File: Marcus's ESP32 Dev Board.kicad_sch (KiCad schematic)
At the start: 55 parts, among them J2 USB_B_Micro, J4 Conn_01x16, U1 ESP32-S3-WROOM-1, U11 BMP390, U4 MMC5983MA, U6 DRV2605LDGS, U7 DRV2605LDGS, U8 MAX17048G_T10, U9 USBLC6-2SC6

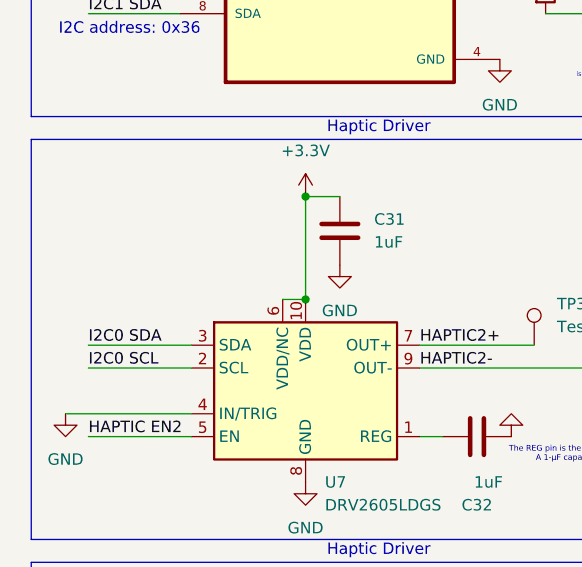
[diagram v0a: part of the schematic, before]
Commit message: feat(pcb) add pullups to I2C0, move battery sensor to I2C0
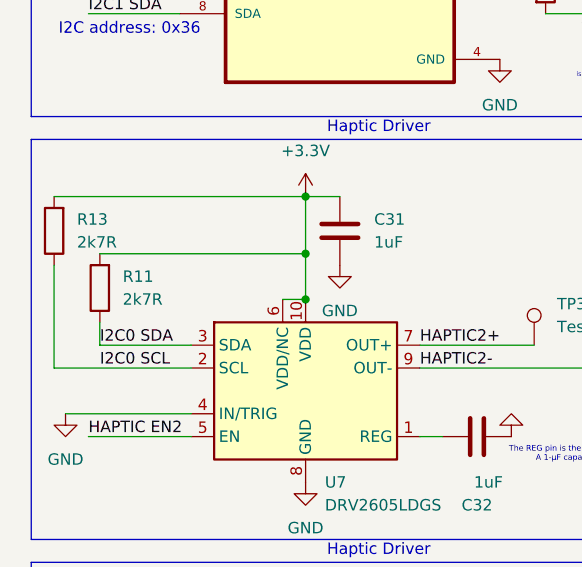
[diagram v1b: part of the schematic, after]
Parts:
- added R11, R13: 2k7R, Capacitor_SMD:C_0402_1005Metric, symbol Device:R
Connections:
- net +3.3V: now also R11.2, R13.2
- net I2C0 SCL: now also R13.1
- net I2C0 SDA: now also R11.1

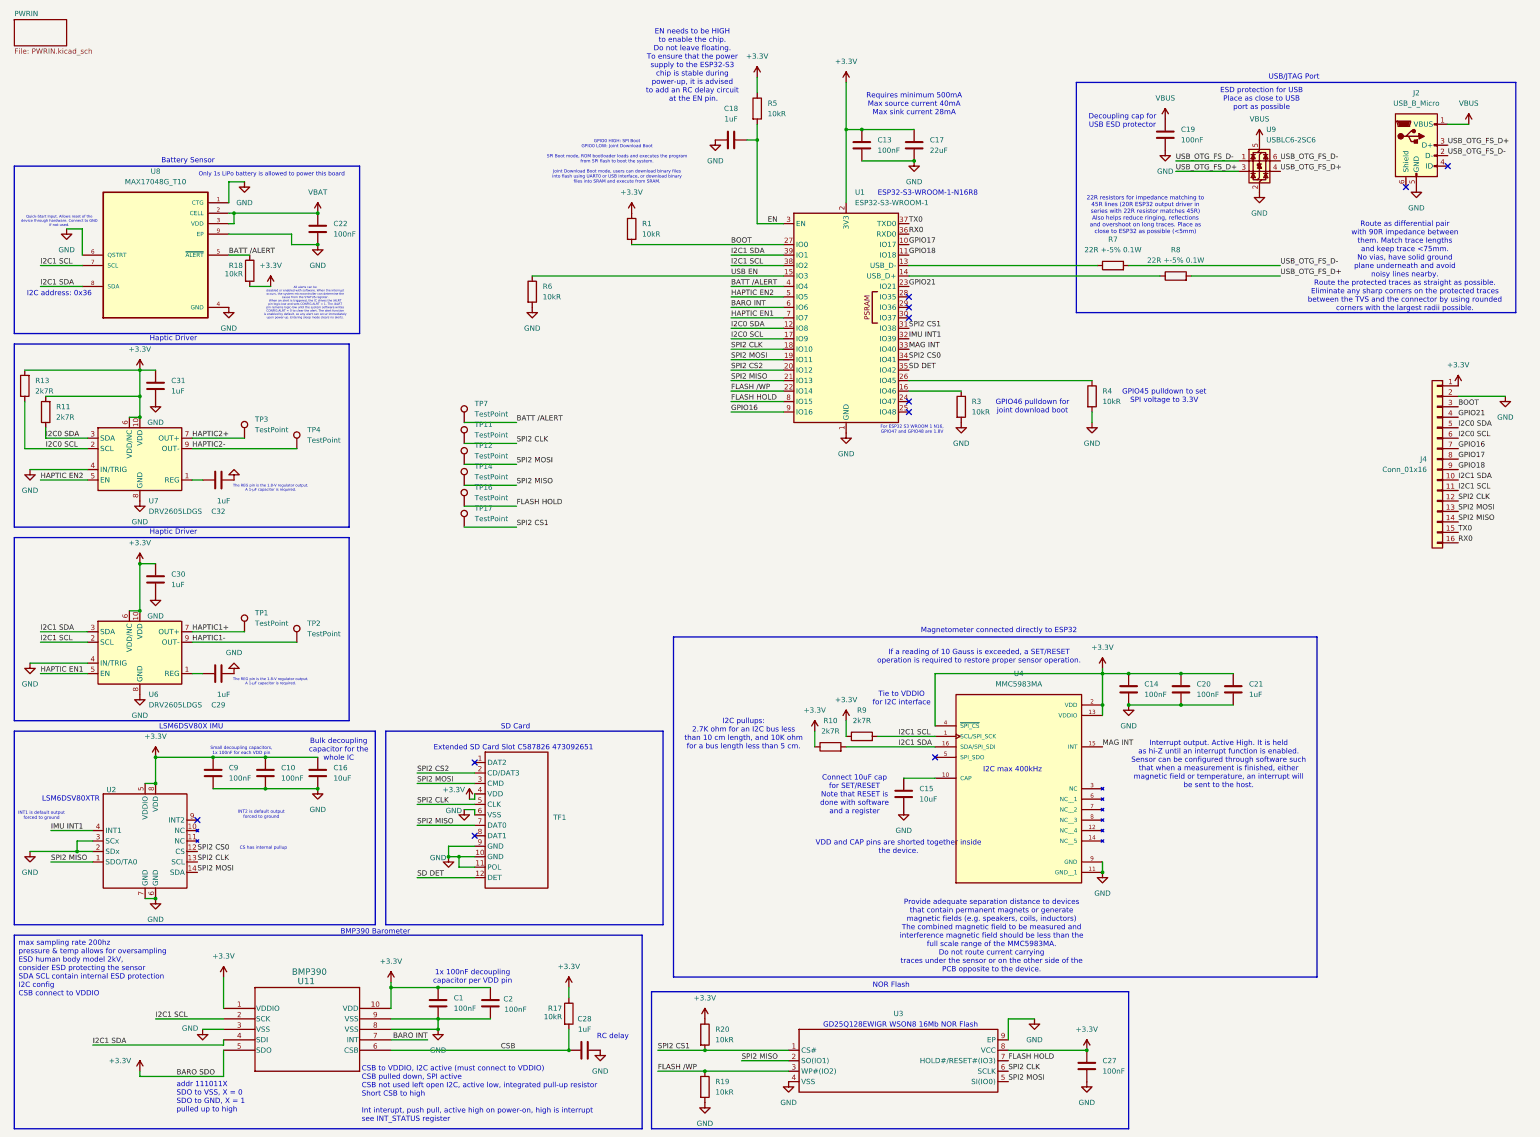
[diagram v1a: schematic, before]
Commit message: feat(pcb) cleanup and improve reliability
add pullups to SPI CS lines, rearrange board slightly, add V1.0 silkscreen, increase size of VBUS input cap
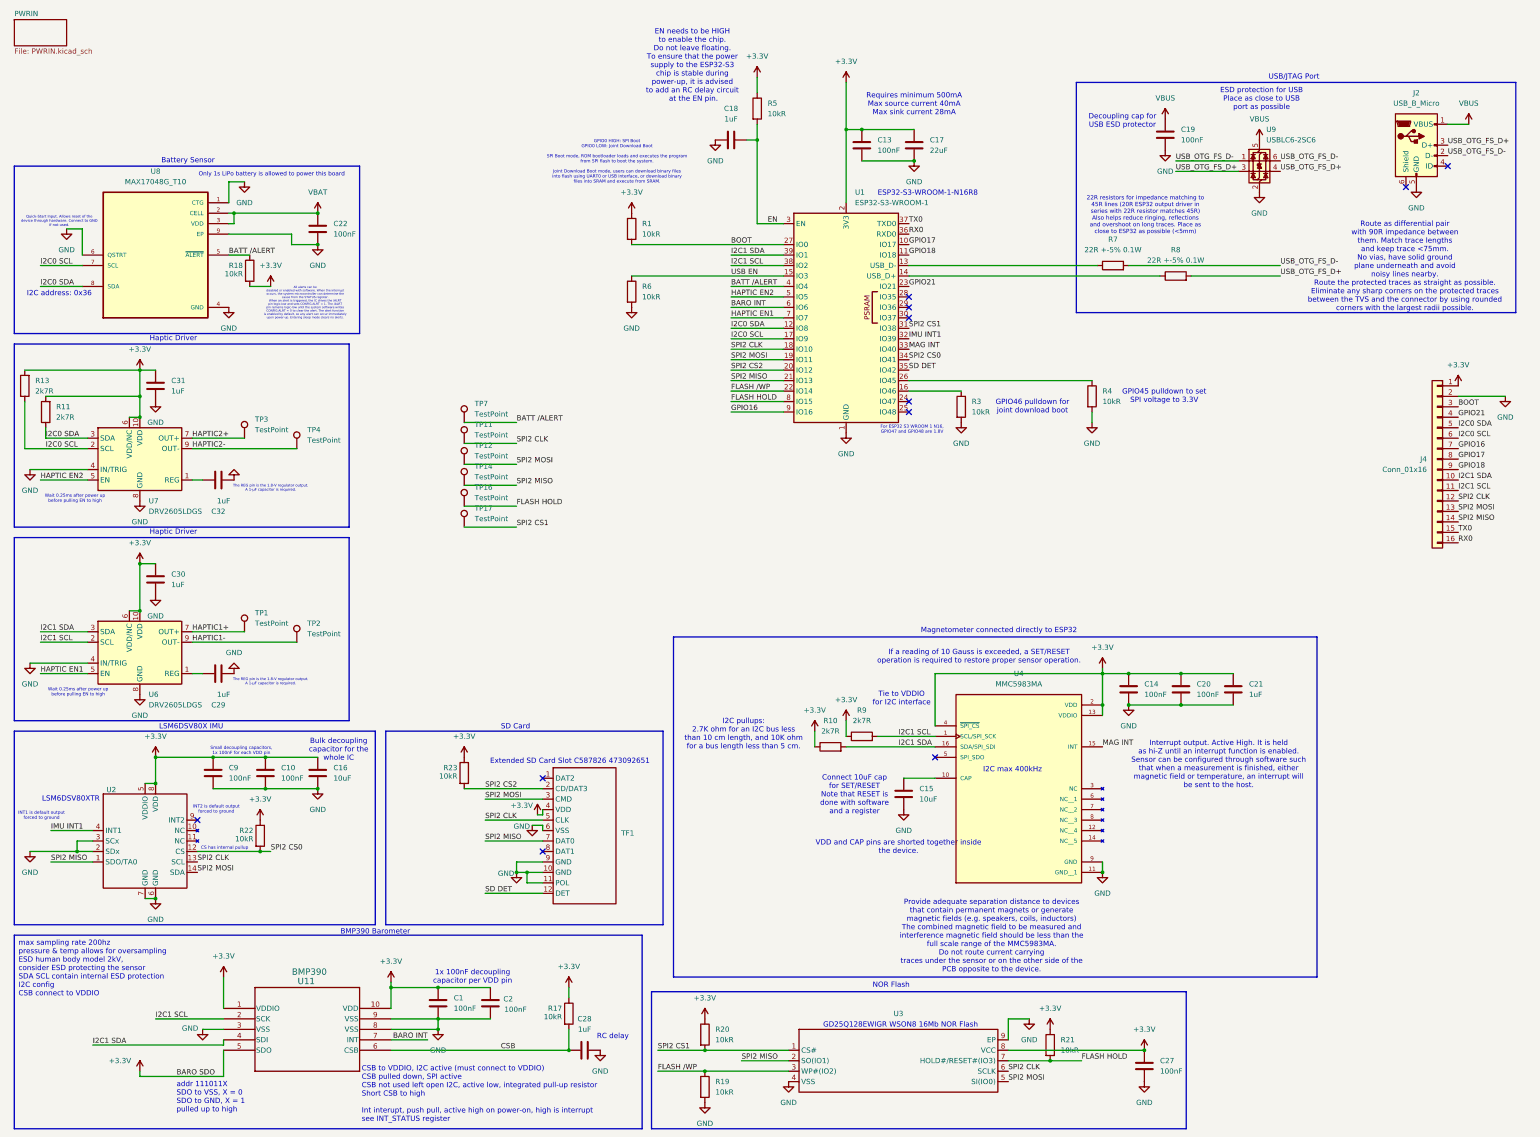
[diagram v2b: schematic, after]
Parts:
- added R21, R22, R23: 10kR, Resistor_SMD:R_0201_0603Metric, symbol Device:R
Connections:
- net +3.3V: now also R21.1, R22.1, R23.1
- net FLASH HOLD: now also R21.2
- net I2C0 SCL: now also U8.7 (SCL)
- net I2C0 SDA: now also U8.8 (SDA)
- net I2C1 SCL: no longer U8.7 (SCL)
- net I2C1 SDA: no longer U8.8 (SDA)
- net SPI2 CS0: now also R22.2
- net SPI2 CS2: now also R23.2
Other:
- note added: "Wait 0.25ms after power up before pulling EN to high"
- moved on the sheet: C27, R6, TF1
